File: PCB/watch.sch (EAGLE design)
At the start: 11 parts, among them IC1 ISL1209, Q1 IRFD9210, U2 MKL27Z256VLH4

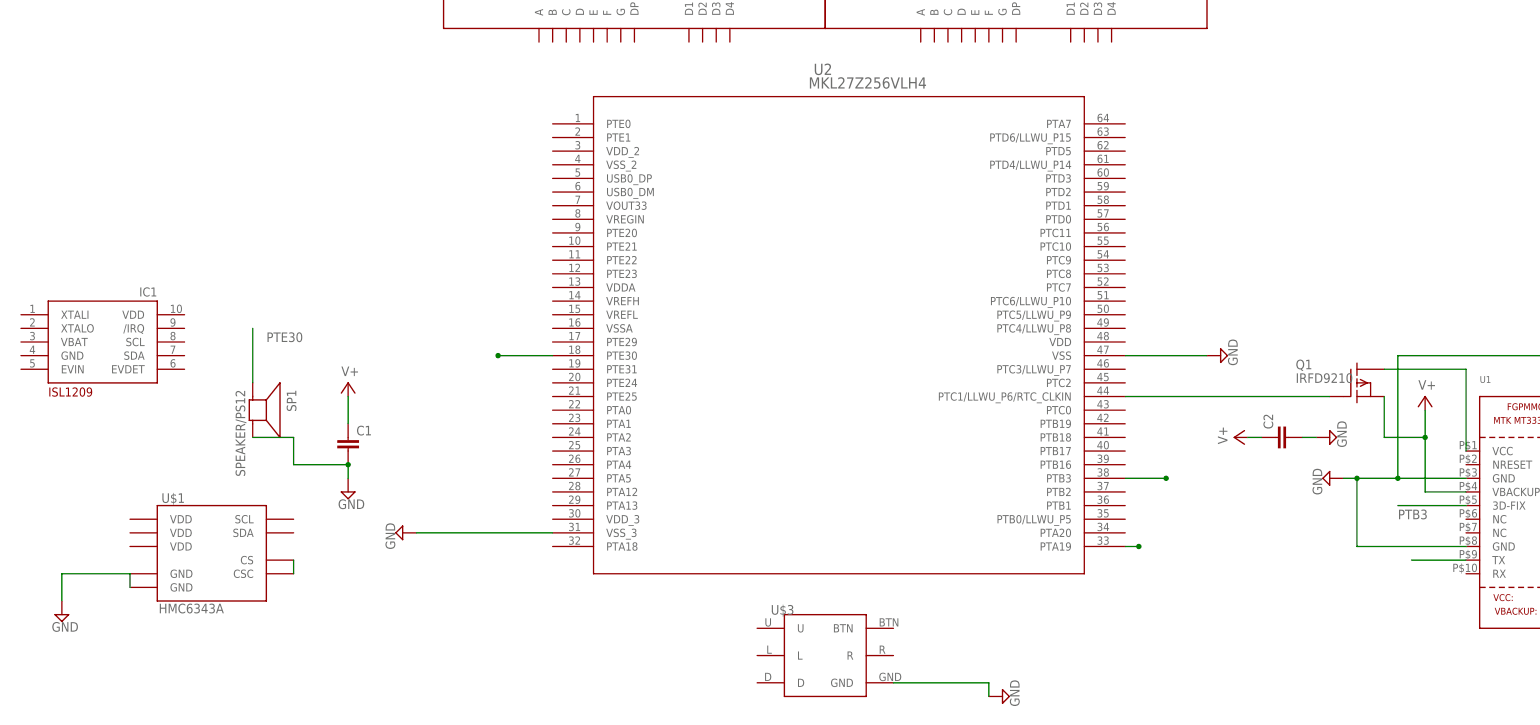
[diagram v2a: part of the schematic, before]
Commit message: wired more components
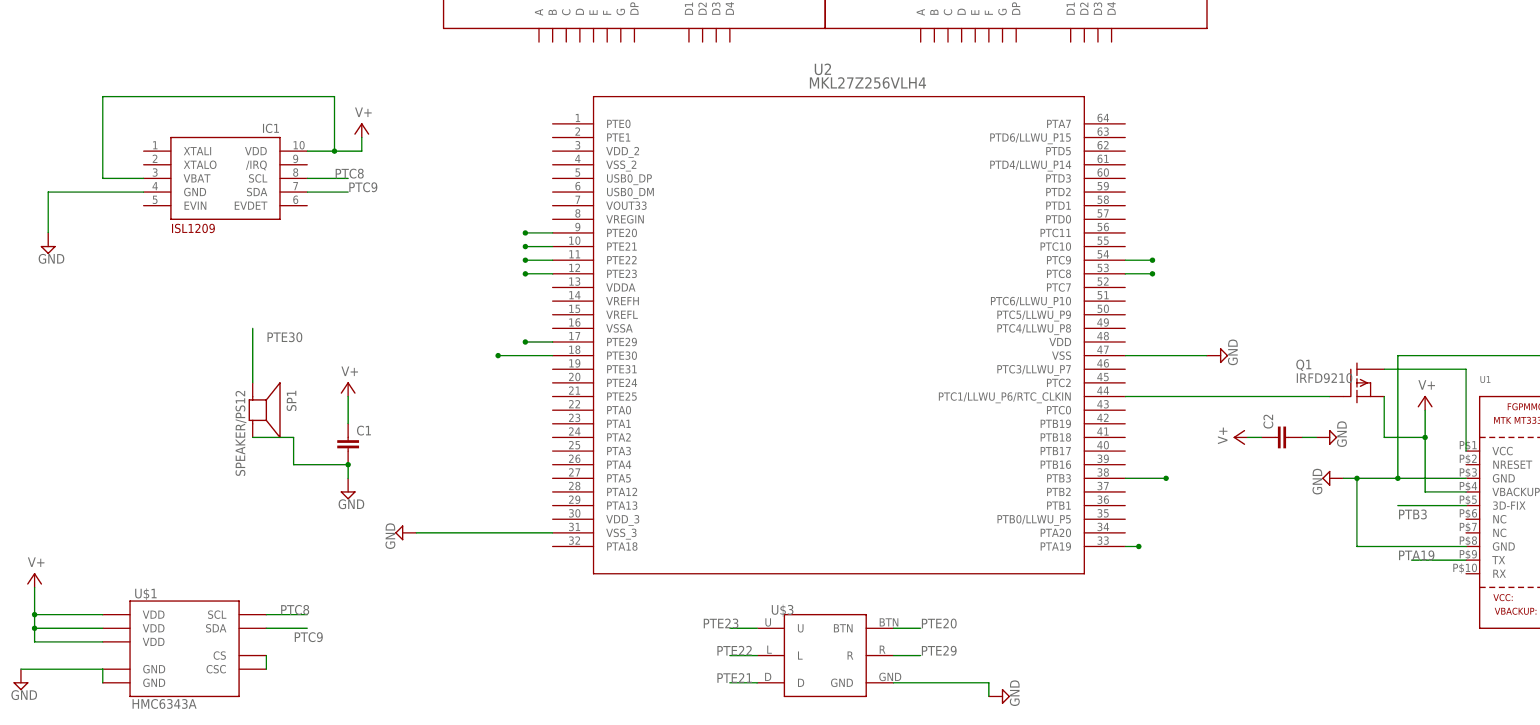
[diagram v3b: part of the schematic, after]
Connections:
- new net PTC8: IC1.SCL, U$1.SCL, U2.PTC8
- new net PTC9: IC1.SDA, U$1.SDA, U2.PTC9
- new net PTE20: U$3.BTN, U2.PTE20
- new net PTE21: U$3.D, U2.PTE21
- new net PTE22: U$3.L, U2.PTE22
- new net PTE23: U$3.U, U2.PTE23
- new net PTE29: U$3.R, U2.PTE29
- net GND: now also IC1.GND
- net V+: now also IC1.VBAT, IC1.VDD, U$1.VDD@11, U$1.VDD@21, U$1.VDD@3
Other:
- moved on the sheet: IC1, U$1
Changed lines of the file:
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@@
 <part name="SP1" library="adafruit" deviceset="SPEAKER" device="/PS12"/>
 <part name="IC1" library="adafruit" deviceset="ISL1209" device=""/>
+<part name="SUPPLY11" library="supply2" deviceset="V+" device=""/>
+<part name="SUPPLY12" library="supply2" deviceset="GND" device=""/>
+<part name="SUPPLY13" library="supply2" deviceset="V+" device=""/>
 </parts>
 <sheets>
@@
 <instance part="DISP1" gate="G$1" x="-10.16" y="195.58"/>
 <instance part="DISP2" gate="G$1" x="60.96" y="195.58"/>
-<instance part="U$1" gate="G$1" x="-88.9" y="83.82"/>
+<instance part="U$1" gate="G$1" x="-93.98" y="66.04"/>
 <instance part="C1" gate="G$1" x="-63.5" y="101.6"/>
-<instance part="SUPPLY1" gate="GND" x="-116.84" y="71.12"/>
+<instance part="SUPPLY1" gate="GND" x="-124.46" y="58.42"/>
 <instance part="SUPPLY2" gate="GND" x="-63.5" y="93.98"/>
 <instance part="SUPPLY3" gate="1" x="-63.5" y="114.3"/>
@@
 <instance part="U$3" gate="G$1" x="25.4" y="63.5"/>
 <instance part="SP1" gate="S1" x="-81.28" y="109.22" rot="R270"/>
-<instance part="IC1" gate="G$1" x="-109.22" y="121.92"/>
+<instance part="IC1" gate="G$1" x="-86.36" y="152.4"/>
+<instance part="SUPPLY11" gate="1" x="-121.92" y="78.74"/>
+<instance part="SUPPLY12" gate="GND" x="-119.38" y="139.7"/>
+<instance part="SUPPLY13" gate="1" x="-60.96" y="162.56"/>
 </instances>
 <busses>
@@
 <pinref part="U$1" gate="G$1" pin="CS"/>
 <pinref part="U$1" gate="G$1" pin="CSC"/>
-<wire x1="-73.66" y1="81.28" x2="-73.66" y2="78.74" width="0.1524" layer="91"/>
+<wire x1="-78.74" y1="63.5" x2="-78.74" y2="60.96" width="0.1524" layer="91"/>
 </segment>
 </net>
@@
 <pinref part="U$1" gate="G$1" pin="GND@25"/>
 <pinref part="U$1" gate="G$1" pin="GND@29"/>
-<wire x1="-104.14" y1="78.74" x2="-104.14" y2="76.2" width="0.1524" layer="91"/>
-<wire x1="-104.14" y1="78.74" x2="-116.84" y2="78.74" width="0.1524" layer="91"/>
+<wire x1="-109.22" y1="60.96" x2="-109.22" y2="58.42" width="0.1524" layer="91"/>
 <pinref part="SUPPLY1" gate="GND" pin="GND"/>
-<wire x1="-116.84" y1="78.74" x2="-116.84" y2="73.66" width="0.1524" layer="91"/>
+<wire x1="-109.22" y1="60.96" x2="-124.46" y2="60.96" width="0.1524" layer="91"/>
 </segment>
 <segment>
@@
 <wire x1="81.28" y1="119.38" x2="96.52" y2="119.38" width="0.1524" layer="91"/>
 </segment>
+<segment>
+<pinref part="IC1" gate="G$1" pin="GND"/>
+<pinref part="SUPPLY12" gate="GND" pin="GND"/>
+<wire x1="-101.6" y1="149.86" x2="-119.38" y2="149.86" width="0.1524" layer="91"/>
+<wire x1="-119.38" y1="149.86" x2="-119.38" y2="142.24" width="0.1524" layer="91"/>
+</segment>
 </net>
 <net name="V+" class="0">
@@
 <junction x="137.16" y="104.14"/>
 </segment>
+<segment>
+<pinref part="SUPPLY11" gate="1" pin="V+"/>
+<wire x1="-121.92" y1="76.2" x2="-121.92" y2="71.12" width="0.1524" layer="91"/>
+<pinref part="U$1" gate="G$1" pin="VDD@11"/>
+<wire x1="-121.92" y1="71.12" x2="-121.92" y2="68.58" width="0.1524" layer="91"/>
+<wire x1="-121.92" y1="68.58" x2="-121.92" y2="66.04" width="0.1524" layer="91"/>
+<wire x1="-121.92" y1="66.04" x2="-109.22" y2="66.04" width="0.1524" layer="91"/>
+<pinref part="U$1" gate="G$1" pin="VDD@21"/>
+<wire x1="-109.22" y1="68.58" x2="-121.92" y2="68.58" width="0.1524" layer="91"/>
+<pinref part="U$1" gate="G$1" pin="VDD@3"/>
+<wire x1="-109.22" y1="71.12" x2="-121.92" y2="71.12" width="0.1524" layer="91"/>
+<junction x="-121.92" y="71.12"/>
+<junction x="-121.92" y="68.58"/>
+</segment>
+<segment>
+<pinref part="IC1" gate="G$1" pin="VDD"/>
+<pinref part="SUPPLY13" gate="1" pin="V+"/>
+<wire x1="-71.12" y1="157.48" x2="-66.04" y2="157.48" width="0.1524" layer="91"/>
+<wire x1="-66.04" y1="157.48" x2="-60.96" y2="157.48" width="0.1524" layer="91"/>
+<wire x1="-60.96" y1="157.48" x2="-60.96" y2="160.02" width="0.1524" layer="91"/>
+<pinref part="IC1" gate="G$1" pin="VBAT"/>
+<wire x1="-101.6" y1="152.4" x2="-109.22" y2="152.4" width="0.1524" layer="91"/>
+<wire x1="-109.22" y1="152.4" x2="-109.22" y2="167.64" width="0.1524" layer="91"/>
+<wire x1="-109.22" y1="167.64" x2="-66.04" y2="167.64" width="0.1524" layer="91"/>
+<wire x1="-66.04" y1="167.64" x2="-66.04" y2="157.48" width="0.1524" layer="91"/>
+<junction x="-66.04" y="157.48"/>
+</segment>
 </net>
 <net name="PTA19" class="0">
@@
 <pinref part="U1" gate="G$1" pin="TX"/>
 <wire x1="144.78" y1="81.28" x2="134.62" y2="81.28" width="0.1524" layer="91"/>
+<label x="132.08" y="81.28" size="1.778" layer="95"/>
 </segment>
 </net>
@@
 </segment>
 </net>
+<net name="PTC8" class="0">
+<segment>
+<pinref part="U2" gate="A" pin="PTC8"/>
+<wire x1="81.28" y1="134.62" x2="86.36" y2="134.62" width="0.1524" layer="91"/>
+<junction x="86.36" y="134.62"/>
+</segment>
+<segment>
+<pinref part="U$1" gate="G$1" pin="SCL"/>
+<wire x1="-78.74" y1="71.12" x2="-71.12" y2="71.12" width="0.1524" layer="91"/>
+<label x="-76.2" y="71.12" size="1.778" layer="95"/>
+</segment>
+<segment>
+<pinref part="IC1" gate="G$1" pin="SCL"/>
+<wire x1="-71.12" y1="152.4" x2="-63.5" y2="152.4" width="0.1524" layer="91"/>
+<label x="-66.04" y="152.4" size="1.778" layer="95"/>
+</segment>
+</net>
+<net name="PTC9" class="0">
+<segment>
+<pinref part="U2" gate="A" pin="PTC9"/>
+<wire x1="81.28" y1="137.16" x2="86.36" y2="137.16" width="0.1524" layer="91"/>
+<junction x="86.36" y="137.16"/>
+</segment>
+<segment>
+<pinref part="U$1" gate="G$1" pin="SDA"/>
+<wire x1="-78.74" y1="68.58" x2="-71.12" y2="68.58" width="0.1524" layer="91"/>
+<label x="-73.66" y="66.04" size="1.778" layer="95"/>
+</segment>
+<segment>
+<pinref part="IC1" gate="G$1" pin="SDA"/>
+<wire x1="-71.12" y1="149.86" x2="-63.5" y2="149.86" width="0.1524" layer="91"/>
+<label x="-63.5" y="149.86" size="1.778" layer="95"/>
+</segment>
+</net>
+<net name="PTE20" class="0">
+<segment>
+<pinref part="U2" gate="A" pin="PTE20"/>
+<wire x1="-25.4" y1="142.24" x2="-30.48" y2="142.24" width="0.1524" layer="91"/>
+<junction x="-30.48" y="142.24"/>
+</segment>
+<segment>
+<pinref part="U$3" gate="G$1" pin="BTN"/>
+<wire x1="38.1" y1="68.58" x2="43.18" y2="68.58" width="0.1524" layer="91"/>
+<label x="43.18" y="68.58" size="1.778" layer="95"/>
+</segment>
+</net>
+<net name="PTE21" class="0">
+<segment>
+<pinref part="U2" gate="A" pin="PTE21"/>
+<wire x1="-25.4" y1="139.7" x2="-30.48" y2="139.7" width="0.1524" layer="91"/>
+<junction x="-30.48" y="139.7"/>
+</segment>
+<segment>
+<pinref part="U$3" gate="G$1" pin="D"/>
+<wire x1="12.7" y1="58.42" x2="7.62" y2="58.42" width="0.1524" layer="91"/>
+<label x="5.08" y="58.42" size="1.778" layer="95"/>
+</segment>
+</net>
+<net name="PTE22" class="0">
+<segment>
+<pinref part="U2" gate="A" pin="PTE22"/>
+<wire x1="-25.4" y1="137.16" x2="-30.48" y2="137.16" width="0.1524" layer="91"/>
+<junction x="-30.48" y="137.16"/>
+</segment>
+<segment>
+<pinref part="U$3" gate="G$1" pin="L"/>
+<wire x1="12.7" y1="63.5" x2="7.62" y2="63.5" width="0.1524" layer="91"/>
+<label x="5.08" y="63.5" size="1.778" layer="95"/>
+</segment>
+</net>
+<net name="PTE23" class="0">
+<segment>
+<pinref part="U2" gate="A" pin="PTE23"/>
+<wire x1="-25.4" y1="134.62" x2="-30.48" y2="134.62" width="0.1524" layer="91"/>
+<junction x="-30.48" y="134.62"/>
+</segment>
+<segment>
+<pinref part="U$3" gate="G$1" pin="U"/>
+<wire x1="12.7" y1="68.58" x2="7.62" y2="68.58" width="0.1524" layer="91"/>
+<label x="2.54" y="68.58" size="1.778" layer="95"/>
+</segment>
+</net>
+<net name="PTE29" class="0">
+<segment>
+<pinref part="U2" gate="A" pin="PTE29"/>
+<wire x1="-25.4" y1="121.92" x2="-30.48" y2="121.92" width="0.1524" layer="91"/>
+<junction x="-30.48" y="121.92"/>
+</segment>
+<segment>
+<pinref part="U$3" gate="G$1" pin="R"/>
+<wire x1="38.1" y1="63.5" x2="43.18" y2="63.5" width="0.1524" layer="91"/>
+<label x="43.18" y="63.5" size="1.778" layer="95"/>
+</segment>
+</net>

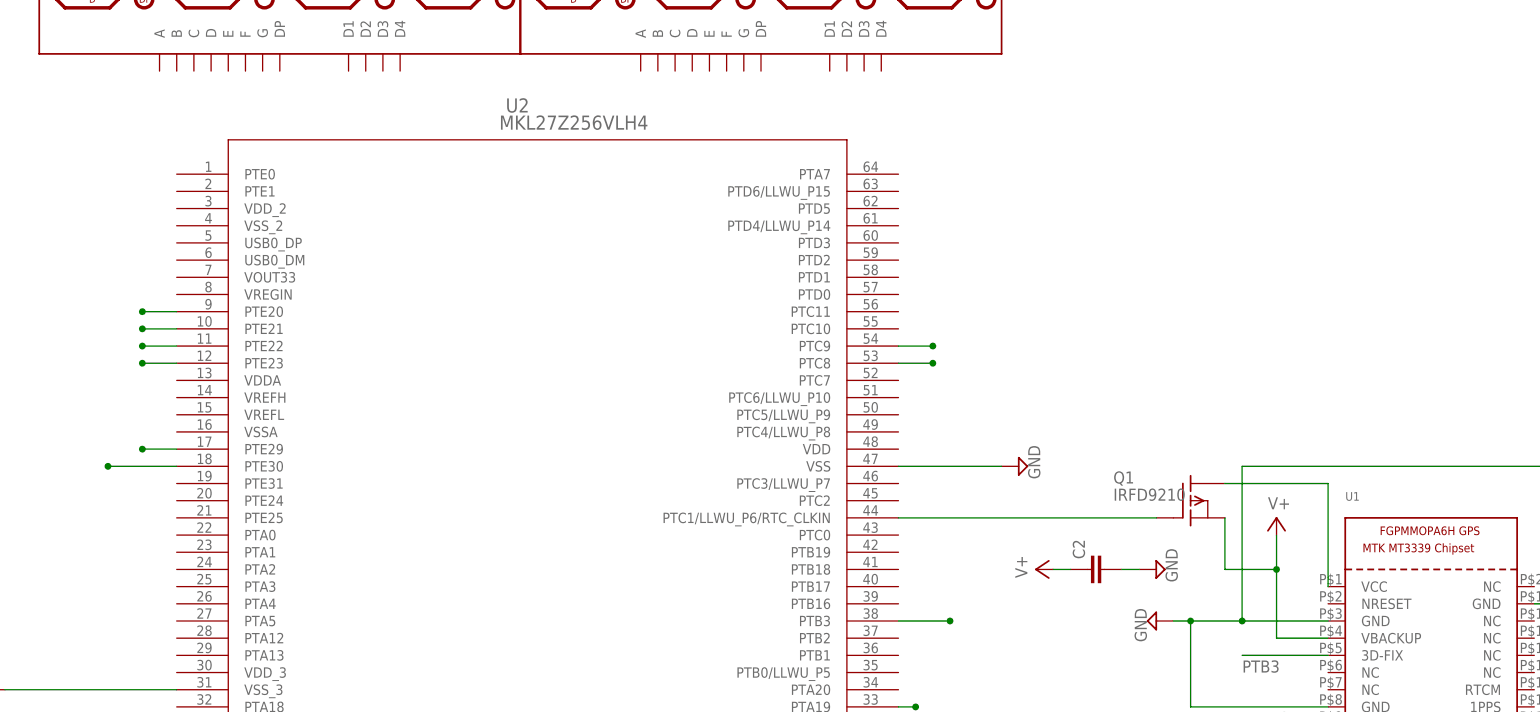
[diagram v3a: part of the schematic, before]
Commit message: added swd breakouts
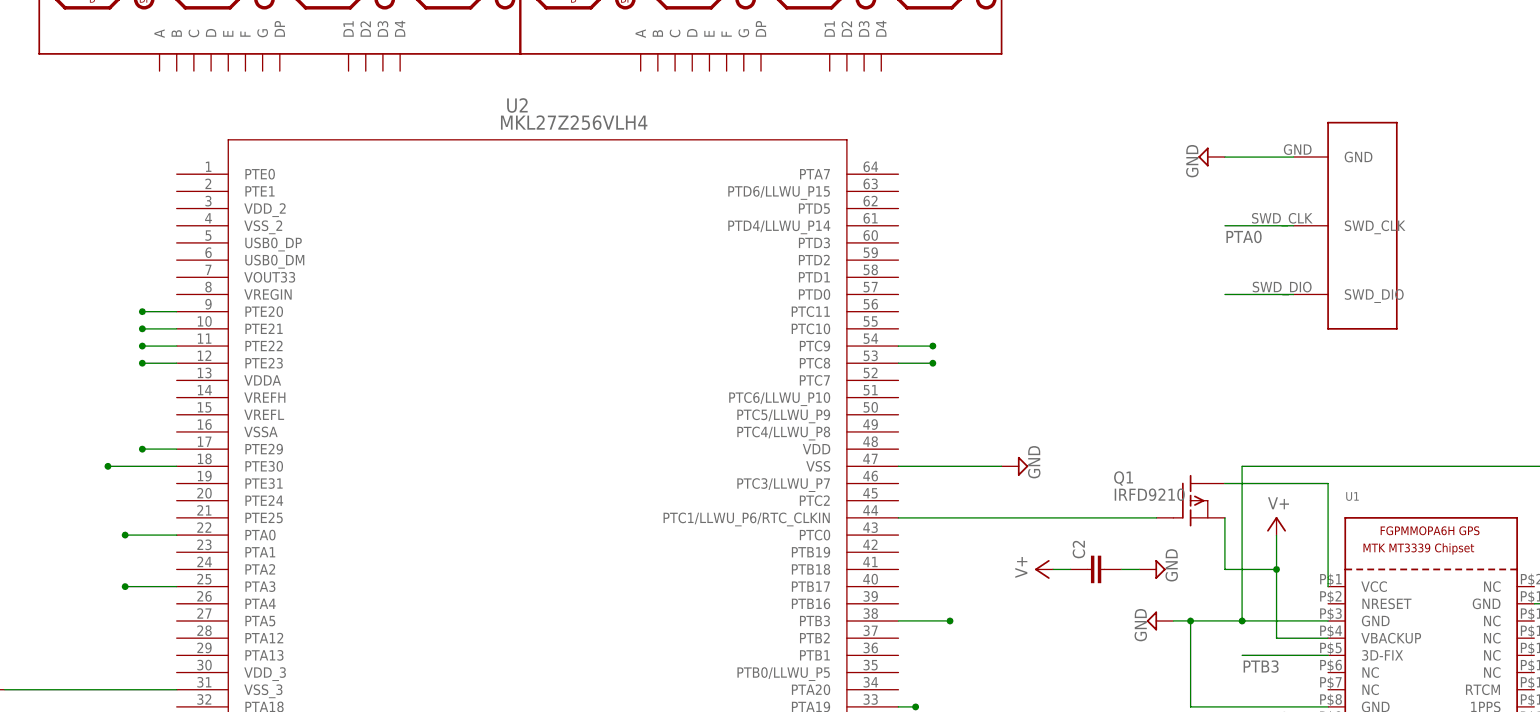
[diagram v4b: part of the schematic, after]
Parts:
- added SWD_BREAKOUT: SWD_BREAKOUTS, BOS_libs:SWD_BREAKOUTS
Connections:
- new net PTA0: SWD_BREAKOUT.SWD_CLK, U2.PTA0
- new net PTA3: SWD_BREAKOUT.SWD_DIO, U2.PTA3
- net GND: now also SWD_BREAKOUT.GND
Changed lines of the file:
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@@
 <part name="SUPPLY12" library="supply2" deviceset="GND" device=""/>
 <part name="SUPPLY13" library="supply2" deviceset="V+" device=""/>
+<part name="SWD_BREAKOUT" library="BOS_libs" deviceset="SWD_BREAKOUTS" device=""/>
+<part name="SUPPLY14" library="supply2" deviceset="GND" device=""/>
 </parts>
 <sheets>
@@
 <instance part="SUPPLY12" gate="GND" x="-119.38" y="139.7"/>
 <instance part="SUPPLY13" gate="1" x="-60.96" y="162.56"/>
+<instance part="SWD_BREAKOUT" gate="G$1" x="149.86" y="157.48" rot="R90"/>
+<instance part="SUPPLY14" gate="GND" x="127" y="165.1" rot="R270"/>
 </instances>
 <busses>
@@
 <wire x1="-119.38" y1="149.86" x2="-119.38" y2="142.24" width="0.1524" layer="91"/>
 </segment>
+<segment>
+<pinref part="SUPPLY14" gate="GND" pin="GND"/>
+<pinref part="SWD_BREAKOUT" gate="G$1" pin="GND"/>
+<wire x1="129.54" y1="165.1" x2="139.7" y2="165.1" width="0.1524" layer="91"/>
+</segment>
 </net>
 <net name="V+" class="0">
@@
 </segment>
 </net>
+<net name="PTA0" class="0">
+<segment>
+<pinref part="SWD_BREAKOUT" gate="G$1" pin="SWD_CLK"/>
+<wire x1="139.7" y1="154.94" x2="129.54" y2="154.94" width="0.1524" layer="91"/>
+<label x="129.54" y="152.4" size="1.778" layer="95"/>
+</segment>
+<segment>
+<pinref part="U2" gate="A" pin="PTA0"/>
+<wire x1="-25.4" y1="109.22" x2="-33.02" y2="109.22" width="0.1524" layer="91"/>
+<junction x="-33.02" y="109.22"/>
+</segment>
+</net>
+<net name="PTA3" class="0">
+<segment>
+<pinref part="U2" gate="A" pin="PTA3"/>
+<wire x1="-25.4" y1="101.6" x2="-33.02" y2="101.6" width="0.1524" layer="91"/>
+<junction x="-33.02" y="101.6"/>
+</segment>
+<segment>
+<pinref part="SWD_BREAKOUT" gate="G$1" pin="SWD_DIO"/>
+<wire x1="139.7" y1="144.78" x2="129.54" y2="144.78" width="0.1524" layer="91"/>
+</segment>
+</net>
